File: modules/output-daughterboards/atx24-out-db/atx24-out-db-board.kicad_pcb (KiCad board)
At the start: 4 copper layers, 81.1 x 16.6 mm, 11 parts, among them J1 ATX24 OUT FIELD, J10 TE 63951-1, J11 TE 63951-1, J12 TE 63951-1, J13 TE 63951-1, J14 TE 63951-1, J15 TE 63951-1, J16 TE 63951-1, J17 TE 63951-1, J18 TE 63951-1, J20 SIGNAL STUB (2x5)

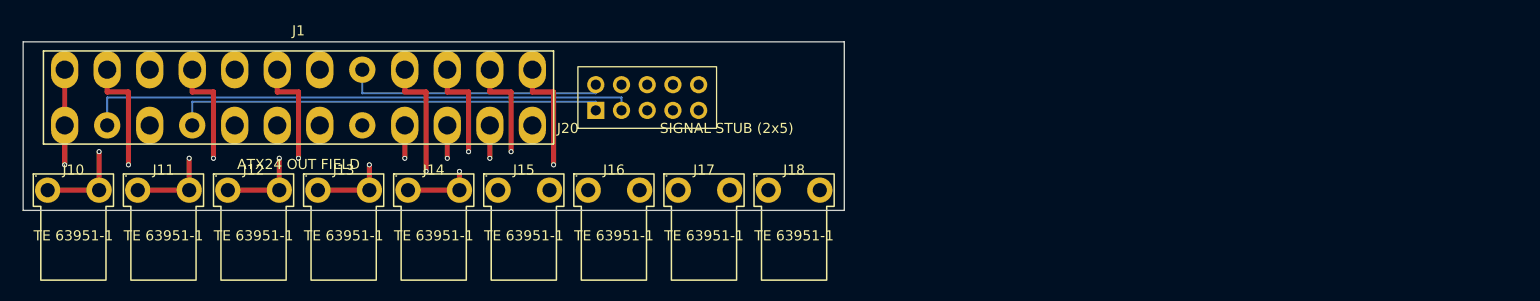
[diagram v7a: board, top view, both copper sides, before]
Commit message: Daughterboard tab form FINAL (owner sketch): 63951-1 legs-vertical, blade-down vertical drop, floating seat — all 3 boards regenerated, gates re-verified
- Part model corrected from TE dwg C=63951 (in-plane L; blade at 2.54-8.89mm face standoff, tip 15.75mm below leg midpoint)
- Boards: atx24 145.1x13.6 / eps 67.8x11.0 / pcie 49.4x11.0 (heights inside the <=15mm cap)
- Seating: board floats 8.4-11mm; full 7.16mm jaw engagement; clip slot rotated perpendicular to wall line (5.72mm standoff); row-fit margins verified at kept pitches
- Coordinator re-verified: ERC 0 x3, DRC 0/0 severity-error x3, checker fully green (incl. new orientation/uniform-height/clip-fit assertions), keying no-subset re-proved, net maps + joint counts 9/6/4 unchanged
- owner-queue: fit-check row updated to the final form; 0.27mm hang-shortfall item retired as obsolete; new sample-check items: 15.75mm chain-dim reading, top-entry drop, 0.84mm tab tolerance

Co-Authored-By: Claude Fable 5 <noreply@anthropic.com>
Claude-Session: https://claude.ai/code/session_01LvfqcnEeuin2oyJQw548EX
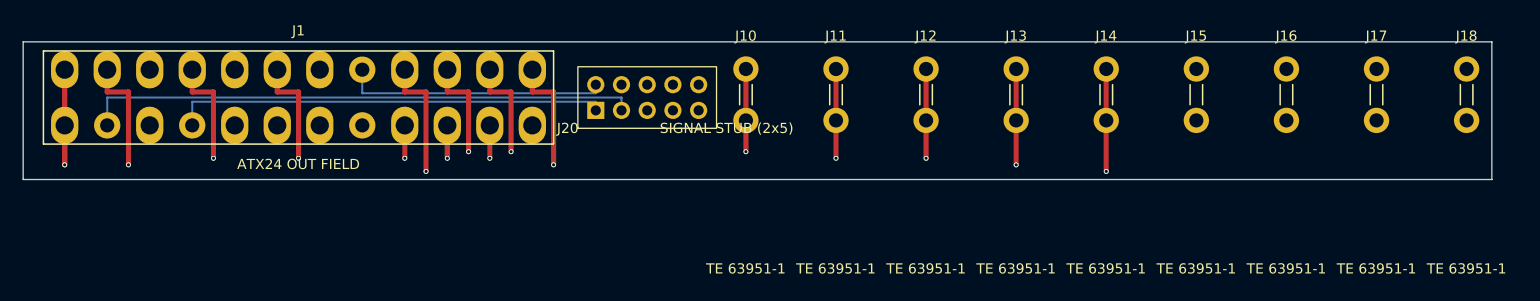
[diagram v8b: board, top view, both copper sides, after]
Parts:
- moved J10 67.1 mm to (71.4, 5.22)
- moved J11 67.1 mm to (80.3, 5.22)
- moved J12 67.1 mm to (89.2, 5.22)
- moved J13 67.1 mm to (98.1, 5.22)
- moved J14 67.1 mm to (107.0, 5.22)
- moved J15 67.1 mm to (115.9, 5.22)
- moved J16 67.1 mm to (124.8, 5.22)
- moved J18 67.1 mm to (142.6, 5.22)
- moved J17 67.1 mm to (133.7, 5.22)
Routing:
- net +5VSB: track 19.1 -> 22.3 mm
- net +3V3: track 43.9 -> 45.8 mm
- net +5V: track 47.9 -> 49.1 mm
- net +12V: track 29.3 -> 28.6 mm
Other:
- board size 81.1 x 16.6 mm -> 145.1 x 13.6 mm
